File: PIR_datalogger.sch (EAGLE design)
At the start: 21 parts, among them J3 FTDI, J4 ISP, Q2 NPN, U1 ATMEGA328P-MU, U8 MCP1703/3.3V, Y1 16MHZ

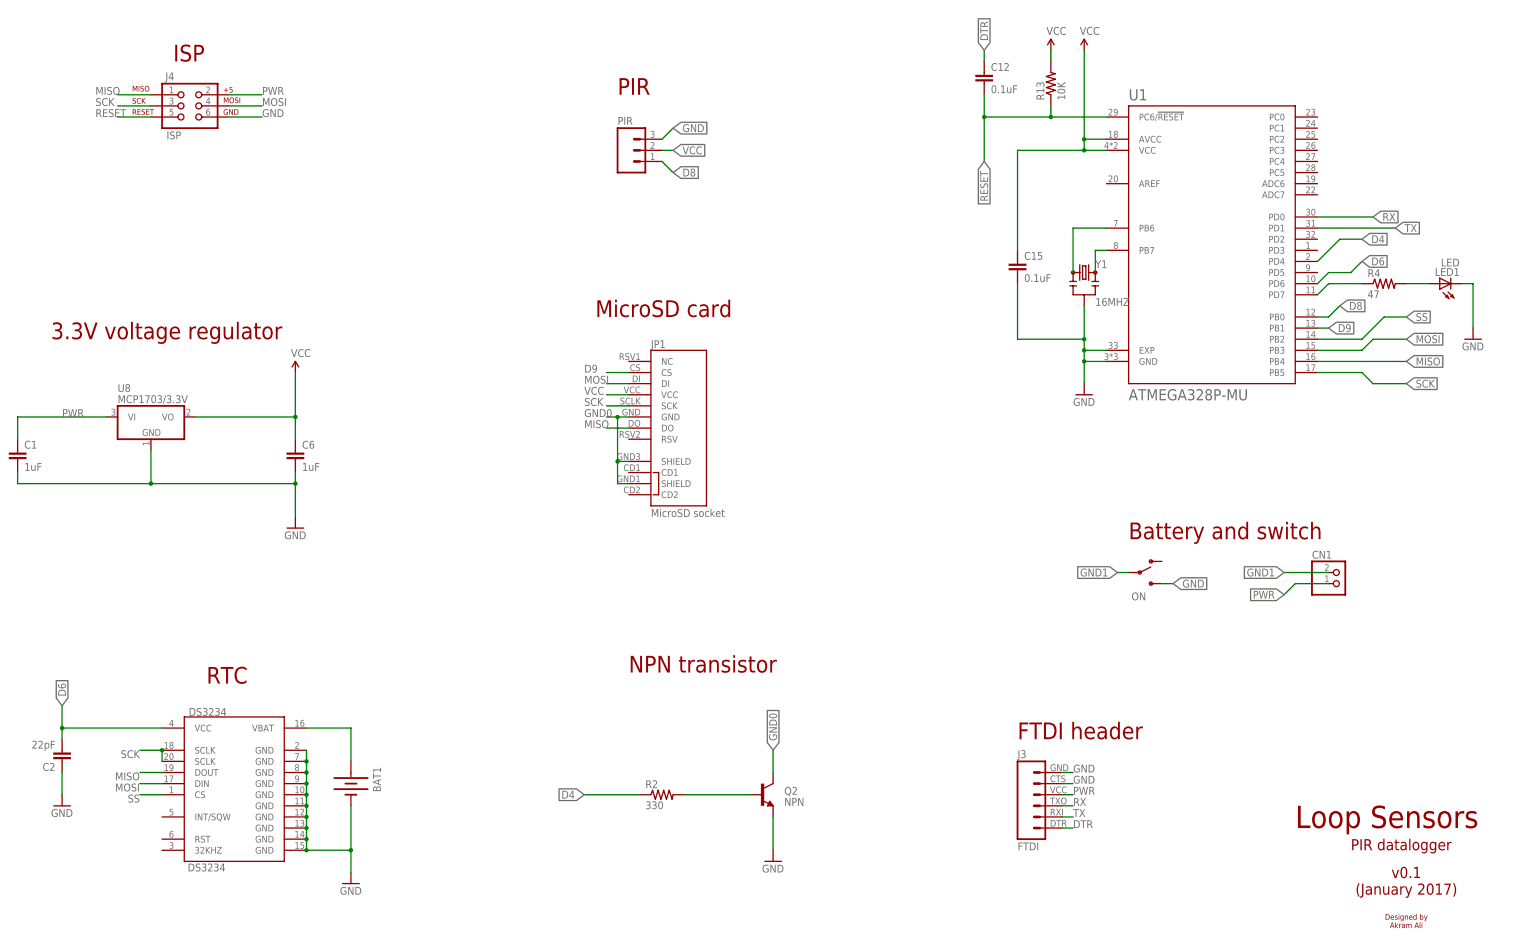
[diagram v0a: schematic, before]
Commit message: v0.2 - design changes
* Removed NPN transistor - microSD cards use their own sleep mode -
keeping up with new SD protocol
* Added decoupling cap to microSD card
* Added pullups to microSD card and RTC
* Adjusted some traces
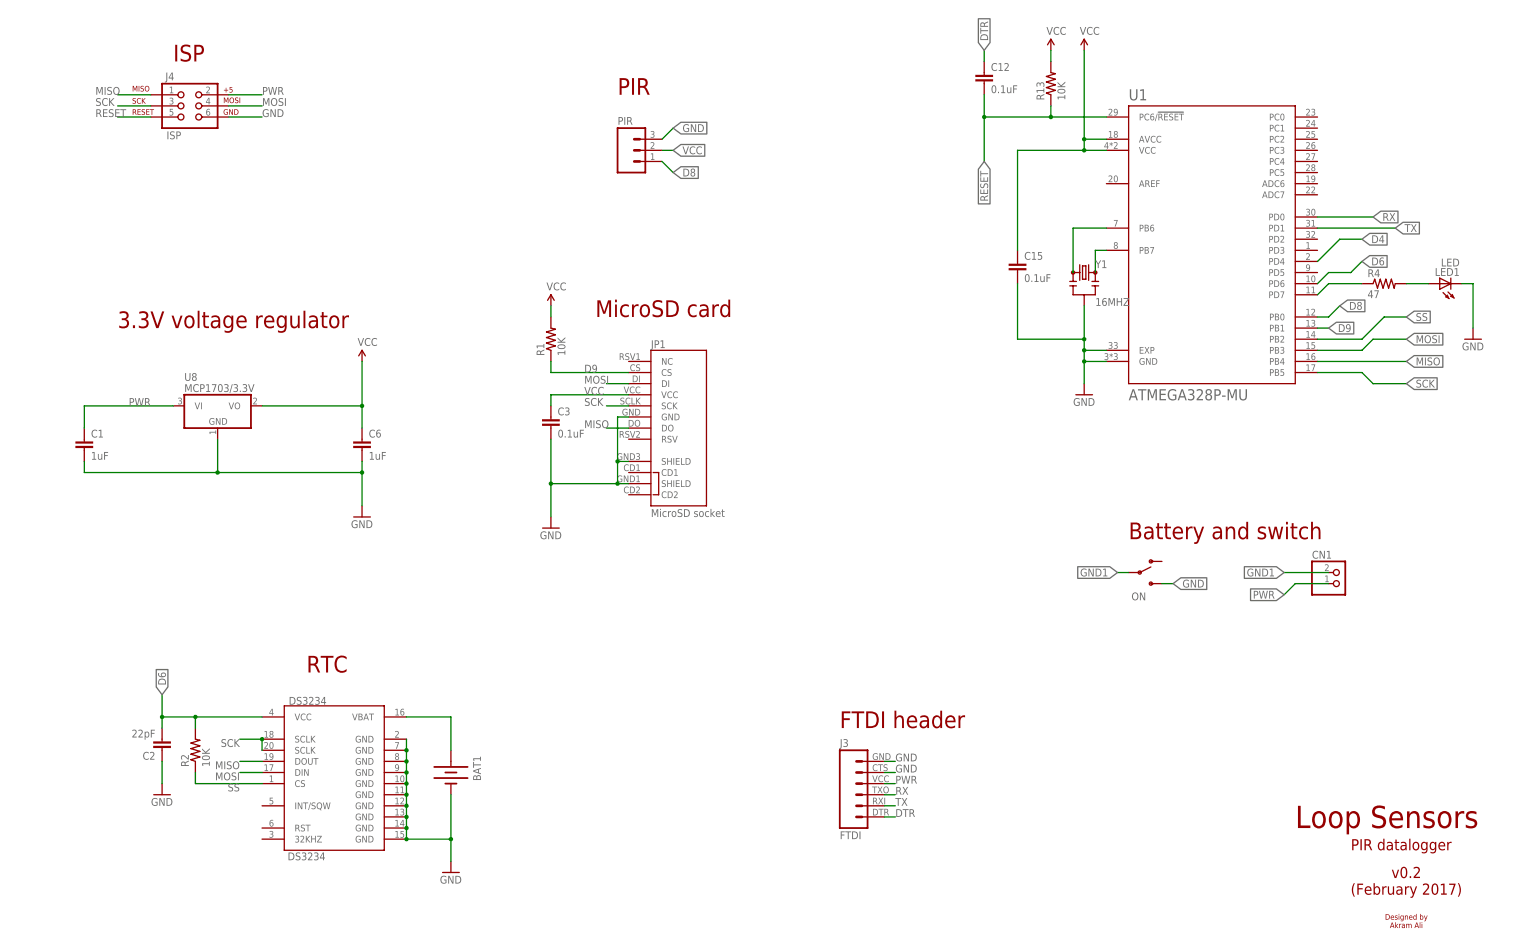
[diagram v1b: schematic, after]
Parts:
- removed Q2: NPN, SparkFun-DiscreteSemi:TRANSISTOR_NPNMMBT5088
- added C3: 0.1uF, SparkFun-Passives:CAP0805
- added R1: 10K, SparkFun-Passives:RESISTOR0805-RES
- R2: value 330 -> 10K; MPN (none) -> RC0805JR-0710KL; OC_NEWARK unknown -> (none)
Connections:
- removed net GND0: JP1.GND, JP1.SHIELD@1, JP1.SHIELD@3, Q2.C
- removed net N$6: Q2.B, R2.2
- net D4: no longer R2.1
- net D6: now also R2.2
- net D9: now also R1.1
- net GND: now also C3.2, JP1.GND, JP1.SHIELD@1, JP1.SHIELD@3; no longer Q2.E
- net SS: now also R2.1
- net VCC: now also C3.1, R1.2
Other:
- note added: "v0.2 (February 2017)"
- note removed: "NPN transistor"
- note removed: "v0.1 (January 2017)"
- moved on the sheet: BAT1, C1, C2, C6, DS3234, J3, R2, U8
